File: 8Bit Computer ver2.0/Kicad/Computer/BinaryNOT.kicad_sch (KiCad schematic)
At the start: 4 parts, among them IC18 SN74AHC74DR, IC19 SN74ABT574ADWR, IC29 SN74LVC1G14DBVR, IC33 SN74LVC1G14DBVR

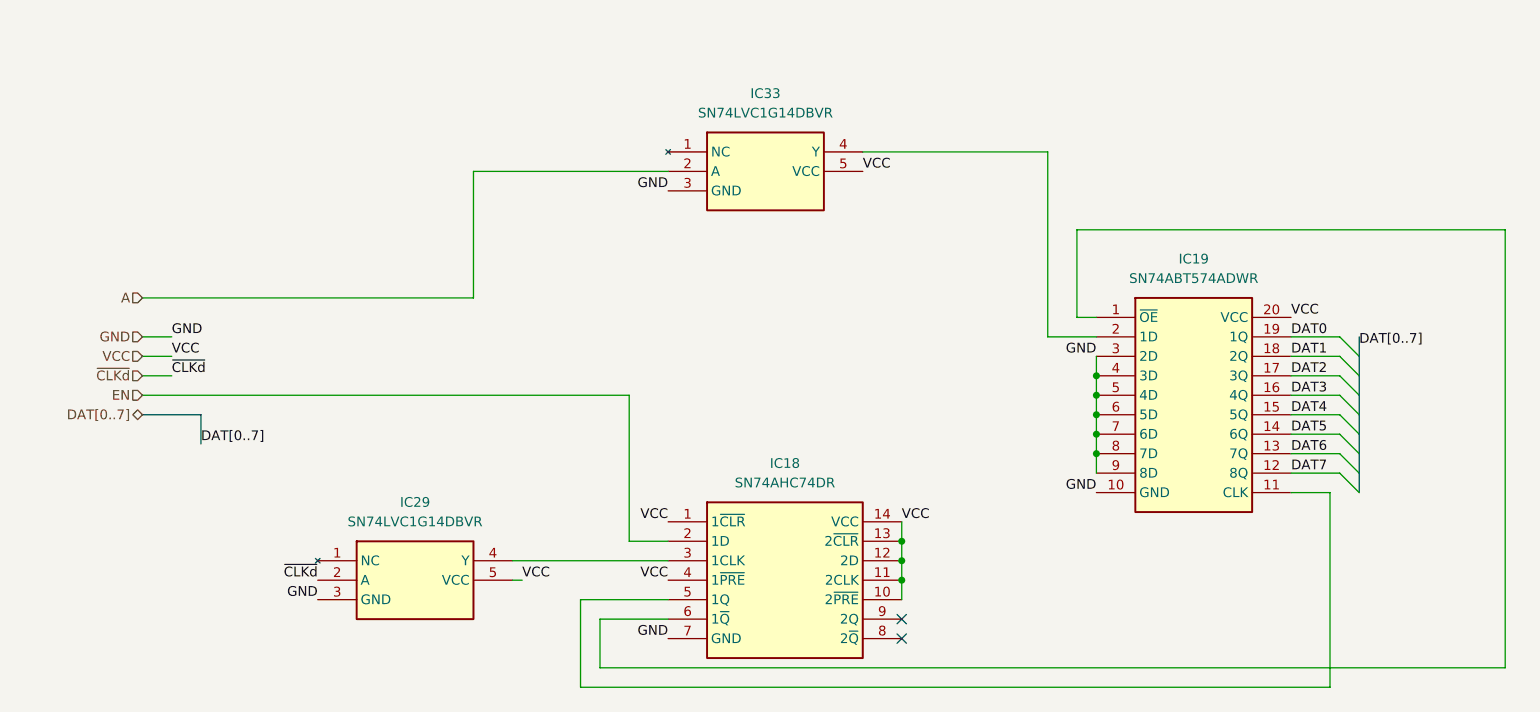
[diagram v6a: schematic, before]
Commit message: Kicad SCH/PCB
Kicad SCH/PCB:
changed the References in SCH
began with INOUTPUT module nearly done
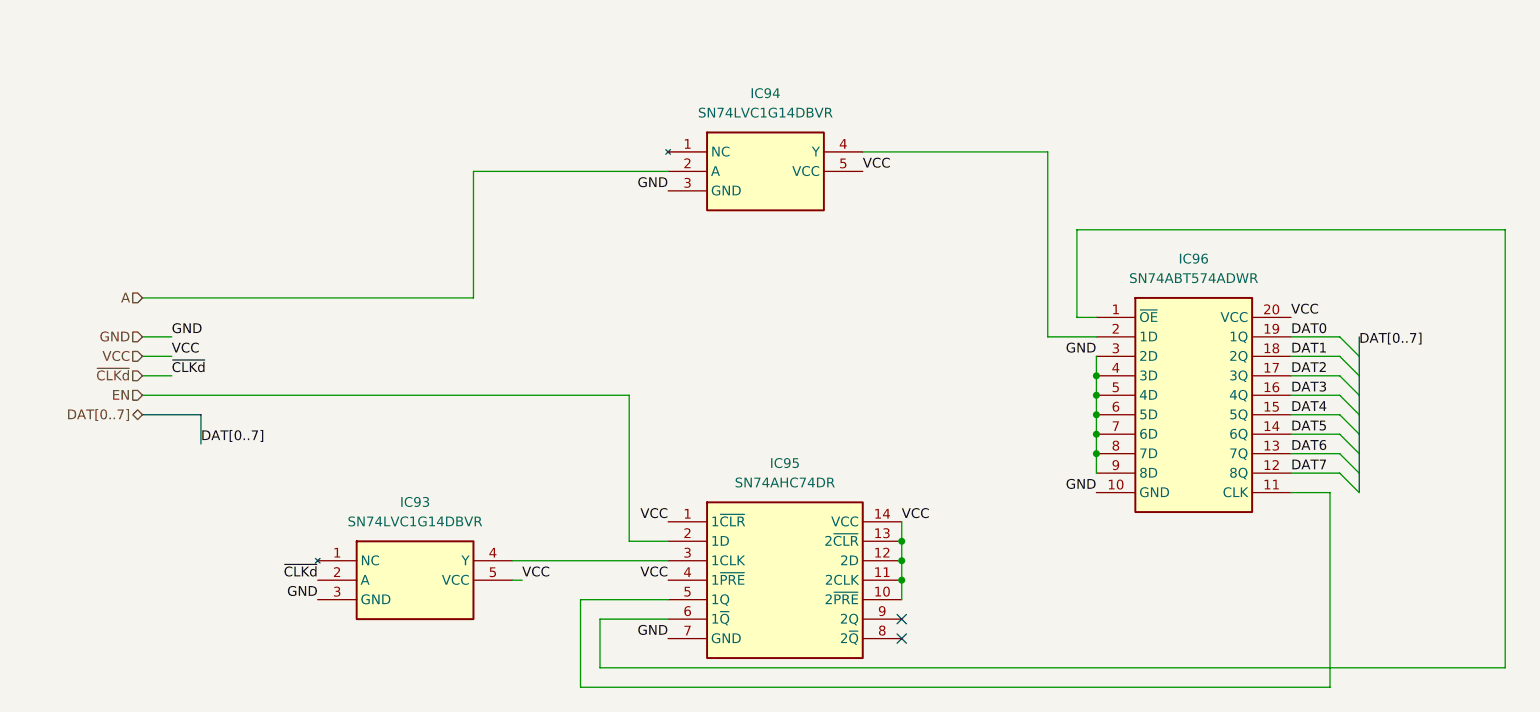
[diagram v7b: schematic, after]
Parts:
- renumbered IC29 to IC93, IC33 to IC94, IC18 to IC95, IC19 to IC96
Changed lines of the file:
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@@
 		(dnp no)
 		(fields_autoplaced yes)
-		(property "Reference" "IC18"
+		(property "Reference" "IC95"
 			(at 139.7 102.87 0)
 			(effects
@@
 			(project "Computer"
 				(path "/1196a00e-6878-4d6d-82b7-9e052dfe7c14/c4d8b530-1c6d-45af-88d2-7dc1d4321a34/5e0e6205-2801-44b7-a427-e7718c49bdd7"
-					(reference "IC18")
+					(reference "IC95")
 					(unit 1)
 				)
@@
 		(dnp no)
 		(fields_autoplaced yes)
-		(property "Reference" "IC33"
+		(property "Reference" "IC94"
 			(at 137.16 54.61 0)
 			(effects
@@
 			(project "Computer"
 				(path "/1196a00e-6878-4d6d-82b7-9e052dfe7c14/c4d8b530-1c6d-45af-88d2-7dc1d4321a34/5e0e6205-2801-44b7-a427-e7718c49bdd7"
-					(reference "IC33")
+					(reference "IC94")
 					(unit 1)
 				)
@@
 		(dnp no)
 		(fields_autoplaced yes)
-		(property "Reference" "IC19"
+		(property "Reference" "IC96"
 			(at 193.04 76.2 0)
 			(effects
@@
 			(project "Computer"
 				(path "/1196a00e-6878-4d6d-82b7-9e052dfe7c14/c4d8b530-1c6d-45af-88d2-7dc1d4321a34/5e0e6205-2801-44b7-a427-e7718c49bdd7"
-					(reference "IC19")
+					(reference "IC96")
 					(unit 1)
 				)
@@
 		(dnp no)
 		(fields_autoplaced yes)
-		(property "Reference" "IC29"
+		(property "Reference" "IC93"
 			(at 91.44 107.95 0)
 			(effects
@@
 			(project "Computer"
 				(path "/1196a00e-6878-4d6d-82b7-9e052dfe7c14/c4d8b530-1c6d-45af-88d2-7dc1d4321a34/5e0e6205-2801-44b7-a427-e7718c49bdd7"
-					(reference "IC29")
+					(reference "IC93")
 					(unit 1)
 				)

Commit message: changed page numbers, compressed ROOT file from A1 to A4
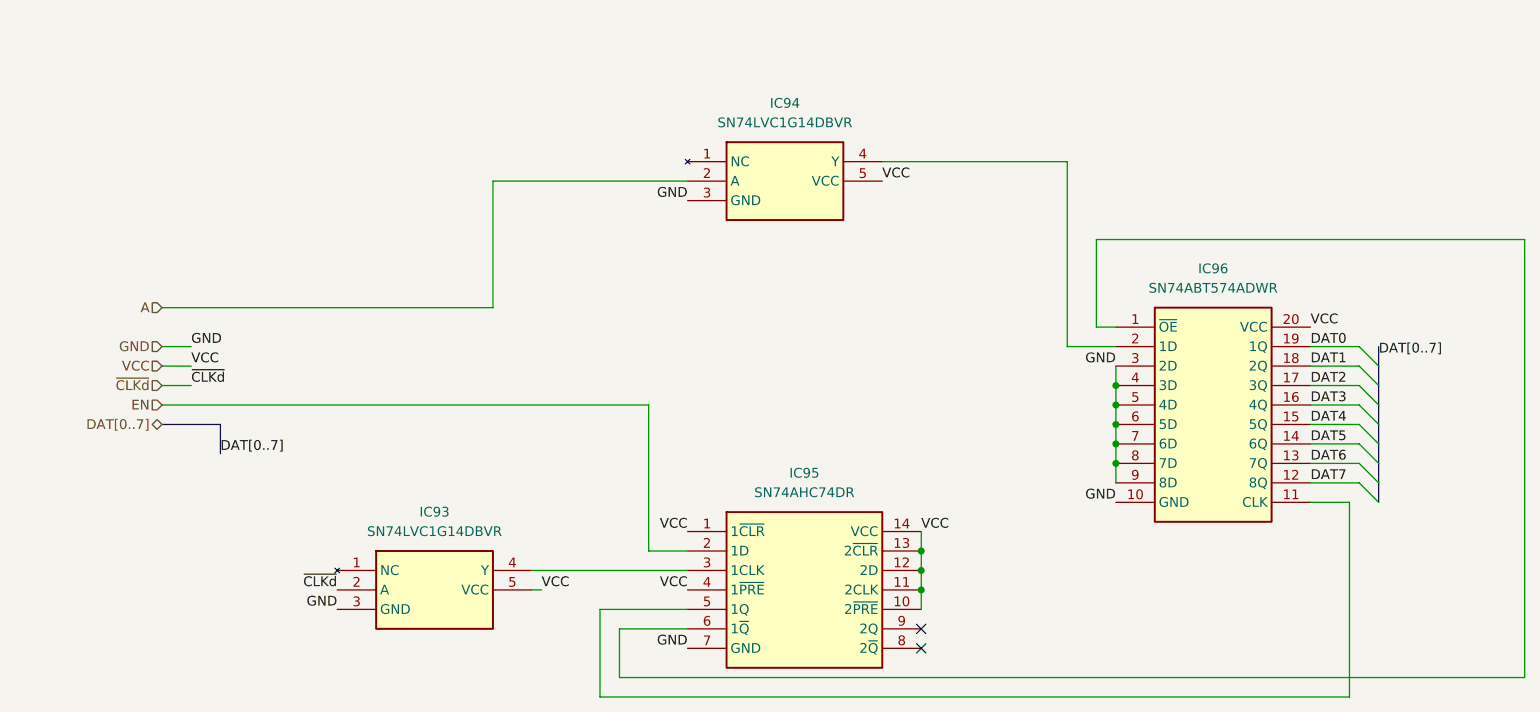
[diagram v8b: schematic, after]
